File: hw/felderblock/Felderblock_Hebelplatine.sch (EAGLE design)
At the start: 35 parts, among them IC3 MCP23017SP

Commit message: last update for mfg
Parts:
- FS1-5, FS2-6, FS3-7, FS4-8: device Jens:SW_2POL_ON-OFF-ONLANGLOCH -> Jens:SW_2POL_ON-OFF-ONSOLDERPAD
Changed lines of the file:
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@@
 </classes>
 <parts>
-<part name="FS1-5" library="Jens" deviceset="SW_2POL_ON-OFF-ON" device="LANGLOCH"/>
-<part name="FS2-6" library="Jens" deviceset="SW_2POL_ON-OFF-ON" device="LANGLOCH"/>
-<part name="FS3-7" library="Jens" deviceset="SW_2POL_ON-OFF-ON" device="LANGLOCH"/>
-<part name="FS4-8" library="Jens" deviceset="SW_2POL_ON-OFF-ON" device="LANGLOCH"/>
+<part name="FS1-5" library="Jens" deviceset="SW_2POL_ON-OFF-ON" device="SOLDERPAD"/>
+<part name="FS2-6" library="Jens" deviceset="SW_2POL_ON-OFF-ON" device="SOLDERPAD"/>
+<part name="FS3-7" library="Jens" deviceset="SW_2POL_ON-OFF-ON" device="SOLDERPAD"/>
+<part name="FS4-8" library="Jens" deviceset="SW_2POL_ON-OFF-ON" device="SOLDERPAD"/>
 <part name="R15" library="resistor" deviceset="R-EU_" device="0207/7" value="10k"/>
 <part name="R16" library="resistor" deviceset="R-EU_" device="0207/7" value="10k"/>
@@
 <instance part="P+4" gate="1" x="208.28" y="111.76"/>
 <instance part="GND11" gate="1" x="127" y="12.7"/>
-<instance part="LED5" gate="D1" x="269.24" y="109.22" rot="R90"/>
-<instance part="LED1" gate="D1" x="269.24" y="99.06" rot="R90"/>
-<instance part="LED6" gate="D1" x="269.24" y="88.9" rot="R90"/>
-<instance part="LED2" gate="D1" x="269.24" y="78.74" rot="R90"/>
-<instance part="LED7" gate="D1" x="269.24" y="68.58" rot="R90"/>
-<instance part="LED3" gate="D1" x="269.24" y="58.42" rot="R90"/>
-<instance part="LED8" gate="D1" x="269.24" y="48.26" rot="R90"/>
-<instance part="LED4" gate="D1" x="269.24" y="38.1" rot="R90"/>
+<instance part="LED5" gate="G$1" x="269.24" y="109.22" rot="R90"/>
+<instance part="LED1" gate="G$1" x="269.24" y="99.06" rot="R90"/>
+<instance part="LED6" gate="G$1" x="269.24" y="88.9" rot="R90"/>
+<instance part="LED2" gate="G$1" x="269.24" y="78.74" rot="R90"/>
+<instance part="LED7" gate="G$1" x="269.24" y="68.58" rot="R90"/>
+<instance part="LED3" gate="G$1" x="269.24" y="58.42" rot="R90"/>
+<instance part="LED8" gate="G$1" x="269.24" y="48.26" rot="R90"/>
+<instance part="LED4" gate="G$1" x="269.24" y="38.1" rot="R90"/>
 <instance part="R23" gate="G$1" x="256.54" y="109.22"/>
 <instance part="R24" gate="G$1" x="256.54" y="99.06"/>
@@
 </segment>
 <segment>
-<pinref part="LED4" gate="D1" pin="C"/>
+<pinref part="LED4" gate="G$1" pin="C"/>
 <pinref part="GND12" gate="1" pin="GND"/>
 <wire x1="274.32" y1="38.1" x2="281.94" y2="38.1" width="0.1524" layer="91"/>
 <wire x1="281.94" y1="38.1" x2="281.94" y2="27.94" width="0.1524" layer="91"/>
-<pinref part="LED8" gate="D1" pin="C"/>
+<pinref part="LED8" gate="G$1" pin="C"/>
 <wire x1="274.32" y1="48.26" x2="281.94" y2="48.26" width="0.1524" layer="91"/>
 <wire x1="281.94" y1="48.26" x2="281.94" y2="38.1" width="0.1524" layer="91"/>
 <junction x="281.94" y="38.1"/>
-<pinref part="LED3" gate="D1" pin="C"/>
+<pinref part="LED3" gate="G$1" pin="C"/>
 <wire x1="274.32" y1="58.42" x2="281.94" y2="58.42" width="0.1524" layer="91"/>
 <wire x1="281.94" y1="58.42" x2="281.94" y2="48.26" width="0.1524" layer="91"/>
 <junction x="281.94" y="48.26"/>
-<pinref part="LED7" gate="D1" pin="C"/>
+<pinref part="LED7" gate="G$1" pin="C"/>
 <wire x1="274.32" y1="68.58" x2="281.94" y2="68.58" width="0.1524" layer="91"/>
 <wire x1="281.94" y1="68.58" x2="281.94" y2="58.42" width="0.1524" layer="91"/>
 <junction x="281.94" y="58.42"/>
-<pinref part="LED2" gate="D1" pin="C"/>
+<pinref part="LED2" gate="G$1" pin="C"/>
 <wire x1="274.32" y1="78.74" x2="281.94" y2="78.74" width="0.1524" layer="91"/>
 <wire x1="281.94" y1="78.74" x2="281.94" y2="68.58" width="0.1524" layer="91"/>
 <junction x="281.94" y="68.58"/>
-<pinref part="LED6" gate="D1" pin="C"/>
+<pinref part="LED6" gate="G$1" pin="C"/>
 <wire x1="274.32" y1="88.9" x2="281.94" y2="88.9" width="0.1524" layer="91"/>
 <wire x1="281.94" y1="88.9" x2="281.94" y2="78.74" width="0.1524" layer="91"/>
 <junction x="281.94" y="78.74"/>
-<pinref part="LED1" gate="D1" pin="C"/>
+<pinref part="LED1" gate="G$1" pin="C"/>
 <wire x1="274.32" y1="99.06" x2="281.94" y2="99.06" width="0.1524" layer="91"/>
 <wire x1="281.94" y1="99.06" x2="281.94" y2="88.9" width="0.1524" layer="91"/>
 <junction x="281.94" y="88.9"/>
-<pinref part="LED5" gate="D1" pin="C"/>
+<pinref part="LED5" gate="G$1" pin="C"/>
 <wire x1="274.32" y1="109.22" x2="281.94" y2="109.22" width="0.1524" layer="91"/>
 <wire x1="281.94" y1="109.22" x2="281.94" y2="99.06" width="0.1524" layer="91"/>
@@
 <segment>
 <pinref part="R23" gate="G$1" pin="2"/>
-<pinref part="LED5" gate="D1" pin="A"/>
+<pinref part="LED5" gate="G$1" pin="A"/>
 <wire x1="261.62" y1="109.22" x2="266.7" y2="109.22" width="0.1524" layer="91"/>
 </segment>
@@
 <segment>
 <pinref part="R24" gate="G$1" pin="2"/>
-<pinref part="LED1" gate="D1" pin="A"/>
+<pinref part="LED1" gate="G$1" pin="A"/>
 <wire x1="261.62" y1="99.06" x2="266.7" y2="99.06" width="0.1524" layer="91"/>
 </segment>
@@
 <segment>
 <pinref part="R25" gate="G$1" pin="2"/>
-<pinref part="LED6" gate="D1" pin="A"/>
+<pinref part="LED6" gate="G$1" pin="A"/>
 <wire x1="261.62" y1="88.9" x2="266.7" y2="88.9" width="0.1524" layer="91"/>
 </segment>
@@
 <segment>
 <pinref part="R26" gate="G$1" pin="2"/>
-<pinref part="LED2" gate="D1" pin="A"/>
+<pinref part="LED2" gate="G$1" pin="A"/>
 <wire x1="261.62" y1="78.74" x2="266.7" y2="78.74" width="0.1524" layer="91"/>
 </segment>
@@
 <segment>
 <pinref part="R27" gate="G$1" pin="2"/>
-<pinref part="LED7" gate="D1" pin="A"/>
+<pinref part="LED7" gate="G$1" pin="A"/>
 <wire x1="261.62" y1="68.58" x2="266.7" y2="68.58" width="0.1524" layer="91"/>
 </segment>
@@
 <segment>
 <pinref part="R28" gate="G$1" pin="2"/>
-<pinref part="LED3" gate="D1" pin="A"/>
+<pinref part="LED3" gate="G$1" pin="A"/>
 <wire x1="261.62" y1="58.42" x2="266.7" y2="58.42" width="0.1524" layer="91"/>
 </segment>
@@
 <segment>
 <pinref part="R29" gate="G$1" pin="2"/>
-<pinref part="LED8" gate="D1" pin="A"/>
+<pinref part="LED8" gate="G$1" pin="A"/>
 <wire x1="261.62" y1="48.26" x2="266.7" y2="48.26" width="0.1524" layer="91"/>
 </segment>
@@
 <segment>
 <pinref part="R30" gate="G$1" pin="2"/>
-<pinref part="LED4" gate="D1" pin="A"/>
+<pinref part="LED4" gate="G$1" pin="A"/>
 <wire x1="261.62" y1="38.1" x2="266.7" y2="38.1" width="0.1524" layer="91"/>
 </segment>

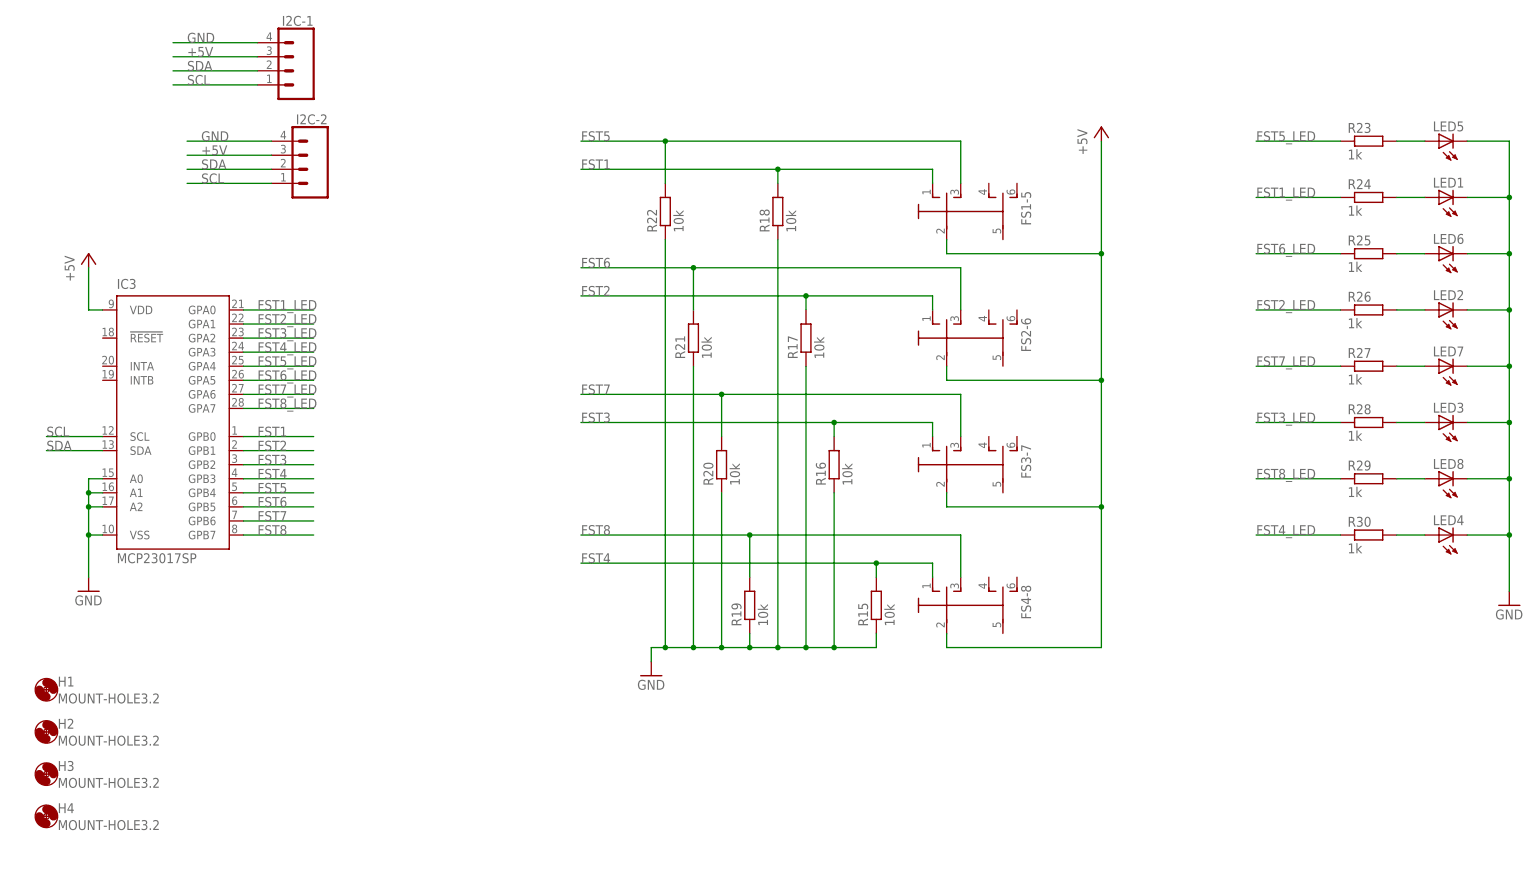
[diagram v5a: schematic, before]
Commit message: moved components to backside
- Components of main panel moved to backside
-  corrected connections for MCP on Hebelplatine
- added address jumpers on Hebelplatine
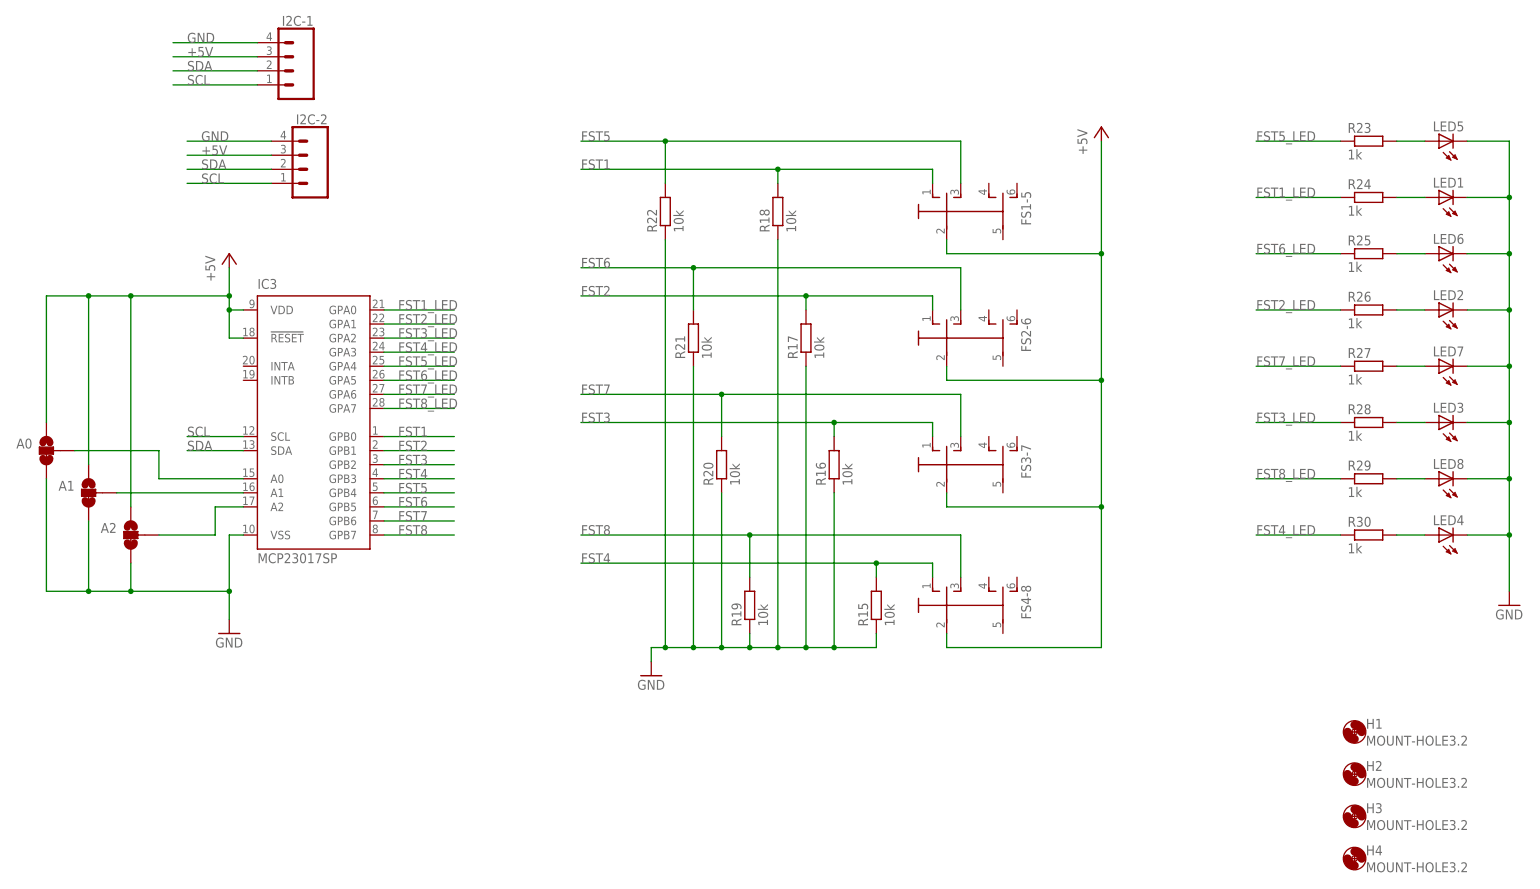
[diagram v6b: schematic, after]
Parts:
- added A0, A1, A2: JUMPER-SMT_3_1-NC_TRACE_SILK, SparkFun-Jumpers:JUMPER-SMT_3_1-NC_TRACE_SILK
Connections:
- new net N$1: A0.2, IC3.A0
- new net N$2: A2.2, IC3.A2
- new net N$3: A1.2, IC3.A1
- net +5V: now also A0.1, A1.1, A2.1, IC3.!RESET
- net GND: now also A0.3, A1.3, A2.3; no longer IC3.A0, IC3.A1, IC3.A2
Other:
- moved on the sheet: H1, H2, H3, H4, IC3

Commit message: Extended to six fields
Extended to six fields per PCB
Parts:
- added R1: 10k, resistor:R-EU_0207/7
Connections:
- new net N$4: IC3.!RESET, R1.1
- net +5V: now also R1.2; no longer IC3.!RESET
- net FST1_LED: now also IC3.GPA7; no longer IC3.GPA0
- net FST2: now also IC3.GPB2; no longer IC3.GPB1
- net FST2_LED: now also IC3.GPA5; no longer IC3.GPA1
- net FST3: now also IC3.GPB4; no longer IC3.GPB2
- net FST3_LED: now also IC3.GPA3; no longer IC3.GPA2
- net FST4: now also IC3.GPB6; no longer IC3.GPB3
- net FST4_LED: now also IC3.GPA1; no longer IC3.GPA3
- net FST5: now also IC3.GPB1; no longer IC3.GPB4
- net FST5_LED: now also IC3.GPA6; no longer IC3.GPA4
- net FST6: now also IC3.GPB3; no longer IC3.GPB5
- net FST6_LED: now also IC3.GPA4; no longer IC3.GPA5
- net FST7: now also IC3.GPB5; no longer IC3.GPB6
- net FST7_LED: now also IC3.GPA2; no longer IC3.GPA6
- net FST8_LED: now also IC3.GPA0; no longer IC3.GPA7
